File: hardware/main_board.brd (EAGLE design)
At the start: 91.4 x 66 mm, 111 parts, among them IC1 IC_USBLC6-2, IC2 LM1117IMPX-3.3, IC3 STM32F107RCT, IC4 DP83848, IC5 LM1117MPX-2.5, U1 USD-SOCKETUSD, U2 VS1003, X2 CRYSTALS-NOGND-CFPX-217, X3 KUSBVX, Y1 CRYSTAL-GROUNDEDSMD-5X3.2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

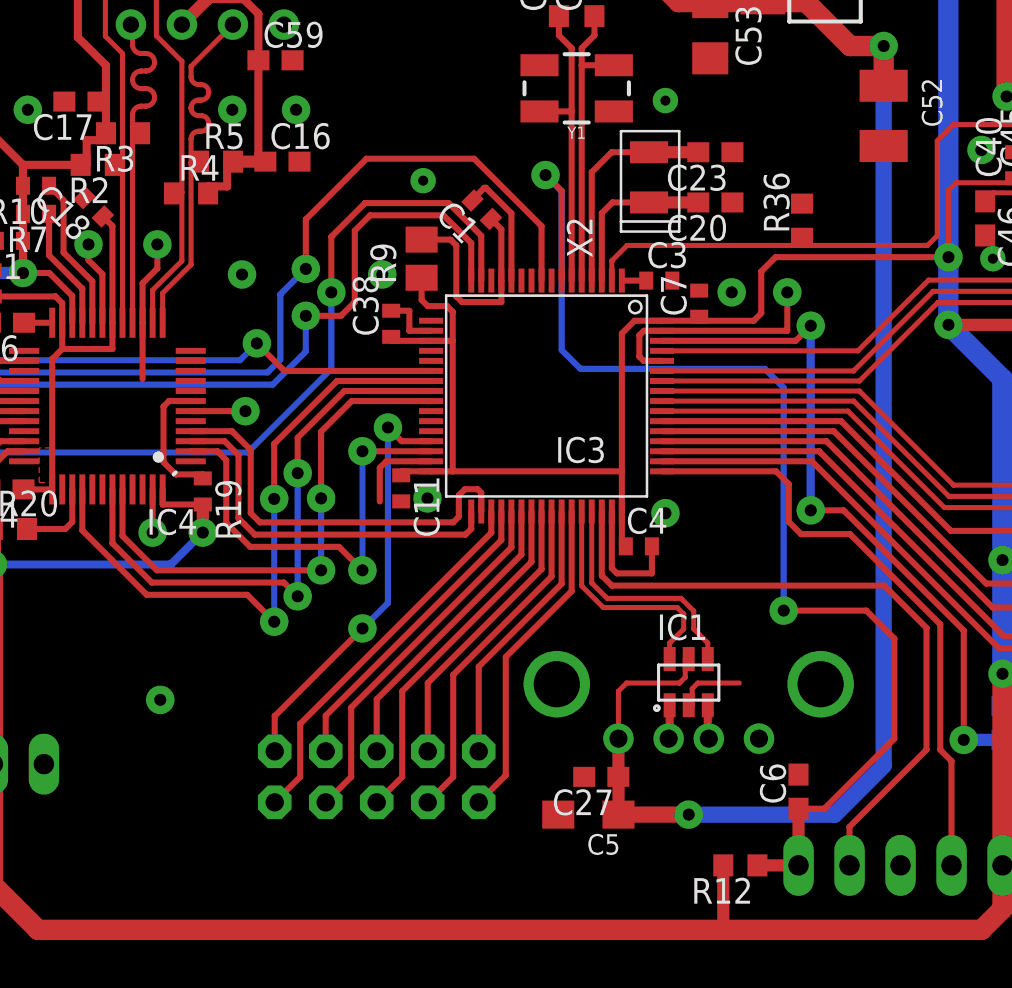
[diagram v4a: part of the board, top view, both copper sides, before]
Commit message: USB overcurrent protection added
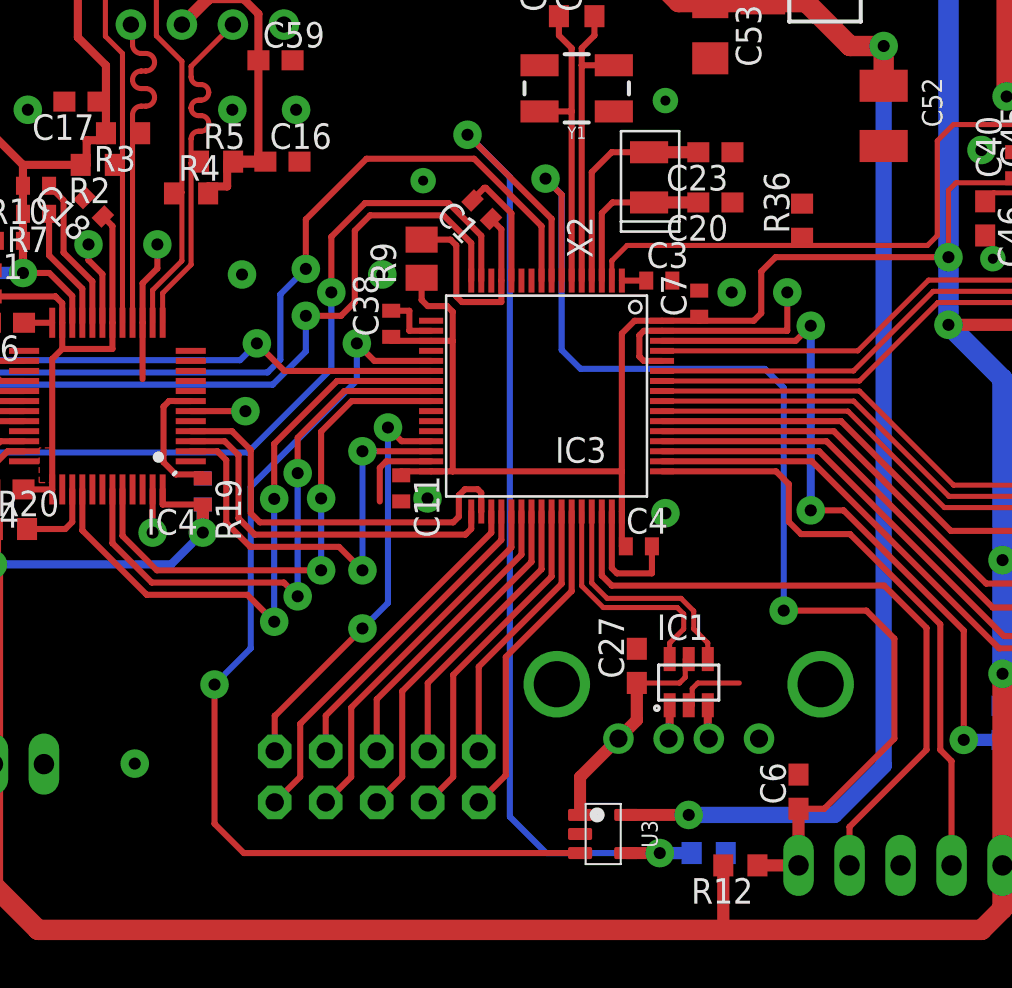
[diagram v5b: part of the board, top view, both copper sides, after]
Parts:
- removed C5: (no value), rcl:SMC_A
- added C8: (no value), rcl:C0402
- added R14: (no value), rcl:R0603
- added U3: (no value), FaBo-Supply:SOT-23-5L
- moved C27 5.80 mm to (45.7, 16.3), turned to 90 degrees
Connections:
- new net 5V: C12.+, C13.1, C52.+, C53.1, F1.2, IC2.3, IC5.3, U3.5
- new net USB_EN: IC3.8, R14.2, U3.4
- new net USB_OVERCURRENT: IC3.21, U3.3
- net 3V: now also C8.1
- net GND: now also C8.2, R14.1, U3.2; no longer C5.-
- net VBUS: now also U3.1; no longer C12.+, C13.1, C5.+, C52.+, C53.1, F1.2, IC2.3, IC5.3
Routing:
- net 5V: track 0.00 -> 77.2 mm, vias 0 -> 2
- net VBUS: track 88.4 -> 11.4 mm, vias 2 -> 0
- net USB_EN: track 0.00 -> 55.3 mm, vias 0 -> 2
- net USB_OVERCURRENT: track 0.00 -> 49.7 mm, vias 0 -> 2
- net 3V: track 447.2 -> 448.6 mm
